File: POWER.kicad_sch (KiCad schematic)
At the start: 40 parts, among them J3 Conn_01x02_Pin, U1 TLV62568DBV, U10 PAM2305AAB250, U11 TLV62569DBV, U12 MIC94093YC6, U4 TLV61070ADBV, U9 BQ24230RGT

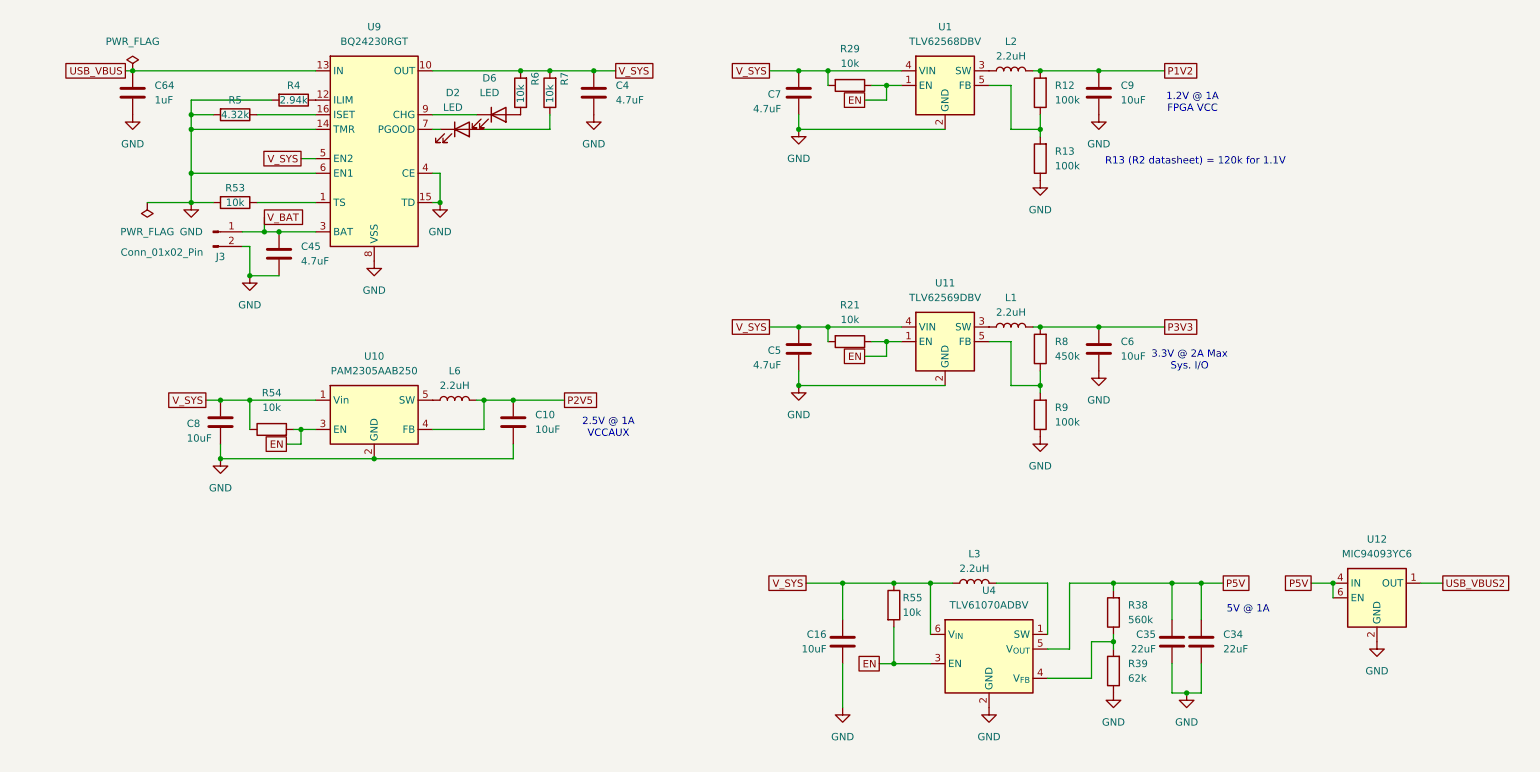
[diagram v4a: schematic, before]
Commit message: End of Version 1.0. Feedback received
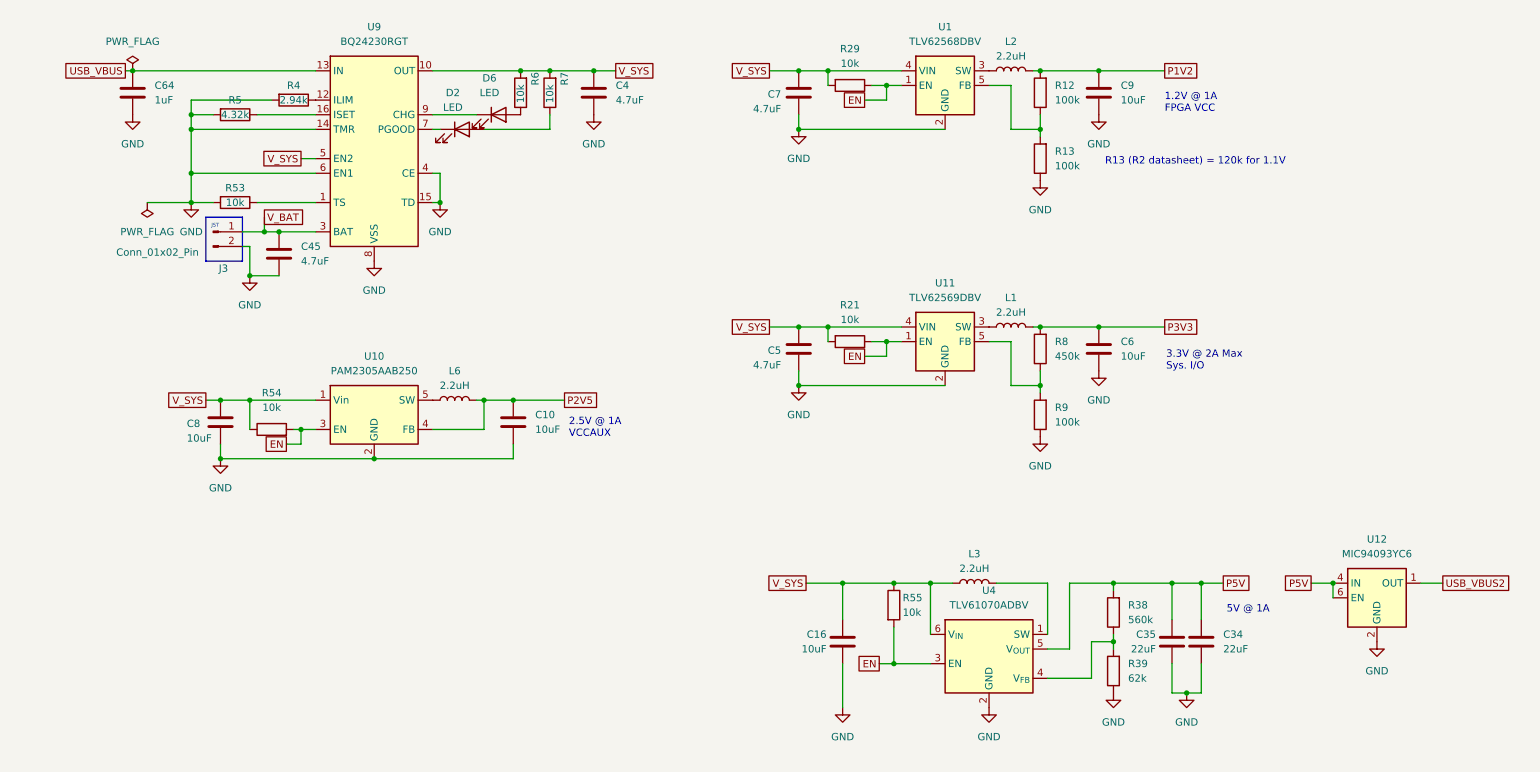
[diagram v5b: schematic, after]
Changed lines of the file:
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@@
 	(text "2.5V @ 1A\nVCCAUX"
 		(exclude_from_sim no)
-		(at 123.19 98.806 0)
+		(at 116.332 98.806 0)
 		(effects
 			(font
 				(size 1.27 1.27)
 			)
+			(justify left)
 		)
 	)
 	(text "3.3V @ 2A Max\nSys. I/O"
 		(exclude_from_sim no)
-		(at 224.028 87.122 0)
+		(at 219.964 87.122 0)
 		(effects
 			(font
 				(size 1.27 1.27)
 			)
+			(justify left)
 		)
 	)
@@
 	(text "1.2V @ 1A\nFPGA VCC"
 		(exclude_from_sim no)
-		(at 224.536 42.418 0)
+		(at 219.71 42.418 0)
 		(effects
 			(font
 				(size 1.27 1.27)
 			)
+			(justify left)
+		)
+	)
+	(text_box "JST"
+		(exclude_from_sim no)
+		(at 53.34 62.23 0)
+		(size 6.35 7.62)
+		(margins 0.9525 0.9525 0.9525 0.9525)
+		(stroke
+			(width 0)
+			(type solid)
+		)
+		(fill
+			(type none)
+		)
+		(effects
+			(font
+				(size 0.635 0.635)
+			)
+			(justify left top)
 		)
 	)
@@
 		(dnp no)
 		(property "Reference" "J3"
-			(at 55.88 69.088 0)
+			(at 56.388 71.12 0)
 			(effects
 				(font
@@
 		)
 		(property "Value" "Conn_01x02_Pin"
-			(at 45.72 68.326 0)
+			(at 44.958 68.326 0)
 			(effects
 				(font
